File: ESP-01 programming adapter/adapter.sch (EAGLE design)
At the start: 7 parts

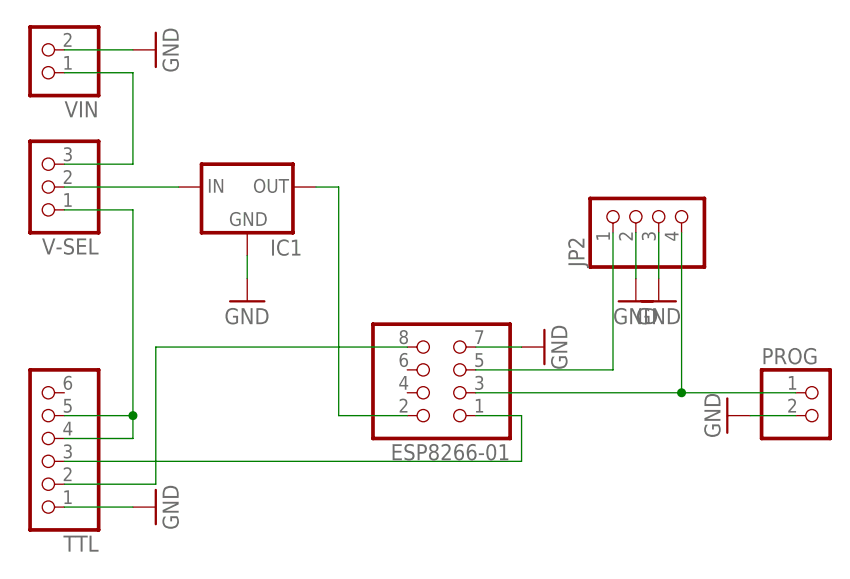
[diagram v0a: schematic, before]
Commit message: CH_PD
Added resistor and jumper to the CH_PD pin, allowing for either
connecting it to VCC for constant on, or to connect it to GPIO00 for
controlling it by code.
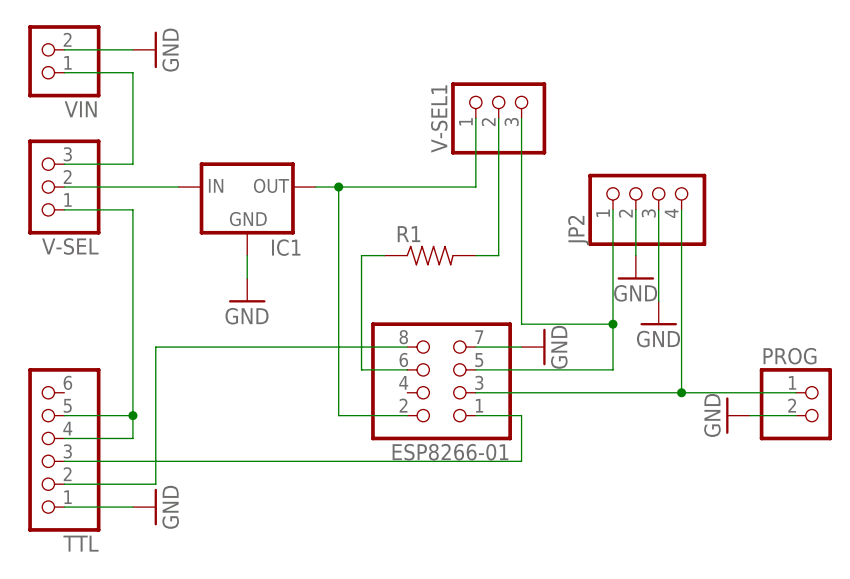
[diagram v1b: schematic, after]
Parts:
- added R1: (no value), SparkFun-Resistors:RESISTORAXIAL-0.3
- added V-SEL1: (no value), pinhead:PINHD-1X3
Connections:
- new net N$10: R1.2, V-SEL1.2
- new net N$8: ESP8266-01.6, R1.1
- net N$1: now also V-SEL1.1
- net N$9: now also V-SEL1.3
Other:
- moved on the sheet: JP2
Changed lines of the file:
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@@
 <part name="GND6" library="supply1" deviceset="GND" device=""/>
 <part name="GND7" library="supply1" deviceset="GND" device=""/>
+<part name="R1" library="SparkFun-Resistors" deviceset="RESISTOR" device="AXIAL-0.3"/>
+<part name="V-SEL1" library="pinhead" deviceset="PINHD-1X3" device=""/>
 </parts>
 <sheets>
@@
 <instance part="VIN" gate="G$1" x="2.54" y="53.34" rot="R180"/>
 <instance part="GND5" gate="1" x="15.24" y="53.34" rot="R90"/>
-<instance part="JP2" gate="A" x="71.12" y="35.56" rot="R90"/>
-<instance part="GND6" gate="1" x="68.58" y="25.4"/>
-<instance part="GND7" gate="1" x="71.12" y="25.4"/>
+<instance part="JP2" gate="A" x="71.12" y="38.1" rot="R90"/>
+<instance part="GND6" gate="1" x="68.58" y="27.94"/>
+<instance part="GND7" gate="1" x="71.12" y="22.86"/>
+<instance part="R1" gate="G$1" x="45.72" y="30.48"/>
+<instance part="V-SEL1" gate="A" x="53.34" y="48.26" rot="R90"/>
 </instances>
 <busses>
@@
 <pinref part="GND6" gate="1" pin="GND"/>
 <pinref part="JP2" gate="A" pin="2"/>
-<wire x1="68.58" y1="27.94" x2="68.58" y2="33.02" width="0.1524" layer="91"/>
+<wire x1="68.58" y1="30.48" x2="68.58" y2="35.56" width="0.1524" layer="91"/>
 </segment>
 <segment>
 <pinref part="GND7" gate="1" pin="GND"/>
 <pinref part="JP2" gate="A" pin="3"/>
-<wire x1="71.12" y1="27.94" x2="71.12" y2="33.02" width="0.1524" layer="91"/>
+<wire x1="71.12" y1="25.4" x2="71.12" y2="35.56" width="0.1524" layer="91"/>
 </segment>
 </net>
@@
 <pinref part="JP2" gate="A" pin="4"/>
 <wire x1="73.66" y1="15.24" x2="50.8" y2="15.24" width="0.1524" layer="91"/>
-<wire x1="73.66" y1="33.02" x2="73.66" y2="15.24" width="0.1524" layer="91"/>
+<wire x1="73.66" y1="35.56" x2="73.66" y2="15.24" width="0.1524" layer="91"/>
 <junction x="73.66" y="15.24"/>
 </segment>
@@
 <pinref part="IC1" gate="G$1" pin="OUT"/>
 <wire x1="35.56" y1="38.1" x2="33.02" y2="38.1" width="0.1524" layer="91"/>
+<wire x1="35.56" y1="38.1" x2="50.8" y2="38.1" width="0.1524" layer="91"/>
+<pinref part="V-SEL1" gate="A" pin="1"/>
+<wire x1="50.8" y1="38.1" x2="50.8" y2="45.72" width="0.1524" layer="91"/>
+<junction x="35.56" y="38.1"/>
 </segment>
 </net>
@@
 <pinref part="JP2" gate="A" pin="1"/>
 <wire x1="50.8" y1="17.78" x2="66.04" y2="17.78" width="0.1524" layer="91"/>
-<wire x1="66.04" y1="17.78" x2="66.04" y2="33.02" width="0.1524" layer="91"/>
+<wire x1="66.04" y1="17.78" x2="66.04" y2="22.86" width="0.1524" layer="91"/>
+<pinref part="V-SEL1" gate="A" pin="3"/>
+<wire x1="66.04" y1="22.86" x2="66.04" y2="35.56" width="0.1524" layer="91"/>
+<wire x1="66.04" y1="22.86" x2="55.88" y2="22.86" width="0.1524" layer="91"/>
+<wire x1="55.88" y1="22.86" x2="55.88" y2="45.72" width="0.1524" layer="91"/>
+<junction x="66.04" y="22.86"/>
 </segment>
 </net>
+<net name="N$8" class="0">
+<segment>
+<pinref part="ESP8266-01" gate="A" pin="6"/>
+<wire x1="43.18" y1="17.78" x2="38.1" y2="17.78" width="0.1524" layer="91"/>
+<wire x1="38.1" y1="17.78" x2="38.1" y2="30.48" width="0.1524" layer="91"/>
+<pinref part="R1" gate="G$1" pin="1"/>
+<wire x1="38.1" y1="30.48" x2="40.64" y2="30.48" width="0.1524" layer="91"/>
+</segment>
+</net>
+<net name="N$10" class="0">
+<segment>
+<pinref part="V-SEL1" gate="A" pin="2"/>
+<wire x1="53.34" y1="45.72" x2="53.34" y2="30.48" width="0.1524" layer="91"/>
+<pinref part="R1" gate="G$1" pin="2"/>
+<wire x1="53.34" y1="30.48" x2="50.8" y2="30.48" width="0.1524" layer="91"/>
+</segment>
+</net>

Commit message: Voltage regulator pin out
Changed pin out on the voltage regulator to fit TI LM1117 TO-220 package

http://www.ti.com/lit/ds/symlink/lm1117-n.pdf
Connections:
- removed net N$6: IC1.IN, V-SEL.2
- new net N$11: IC1.OUT, V-SEL.2
- net GND: now also IC1.IN; no longer IC1.GND
- net N$1: now also IC1.GND; no longer IC1.OUT
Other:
- moved on the sheet: IC1
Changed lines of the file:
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@@
 <part name="ESP8266-01" library="pinhead" deviceset="PINHD-2X4" device=""/>
 <part name="IC1" library="SparkFun-PowerIC" deviceset="V_REG_78XX" device="SIDE"/>
-<part name="GND1" library="supply1" deviceset="GND" device=""/>
 <part name="GND2" library="supply1" deviceset="GND" device=""/>
 <part name="GND3" library="supply1" deviceset="GND" device=""/>
@@
 <part name="R1" library="SparkFun-Resistors" deviceset="RESISTOR" device="AXIAL-0.3"/>
 <part name="V-SEL1" library="pinhead" deviceset="PINHD-1X3" device=""/>
+<part name="GND8" library="supply1" deviceset="GND" device=""/>
 </parts>
 <sheets>
@@
 <instance part="TTL" gate="A" x="2.54" y="10.16" rot="R180"/>
 <instance part="ESP8266-01" gate="A" x="48.26" y="17.78" rot="R180"/>
-<instance part="IC1" gate="G$1" x="25.4" y="38.1"/>
-<instance part="GND1" gate="1" x="25.4" y="25.4"/>
+<instance part="IC1" gate="G$1" x="25.4" y="40.64"/>
 <instance part="GND2" gate="1" x="15.24" y="2.54" rot="R90"/>
 <instance part="GND3" gate="1" x="58.42" y="20.32" rot="R90"/>
@@
 <instance part="R1" gate="G$1" x="45.72" y="30.48"/>
 <instance part="V-SEL1" gate="A" x="53.34" y="48.26" rot="R90"/>
+<instance part="GND8" gate="1" x="17.78" y="30.48"/>
 </instances>
 <busses>
@@
 <nets>
 <net name="GND" class="0">
-<segment>
-<pinref part="GND1" gate="1" pin="GND"/>
-<pinref part="IC1" gate="G$1" pin="GND"/>
-<wire x1="25.4" y1="27.94" x2="25.4" y2="30.48" width="0.1524" layer="91"/>
-</segment>
 <segment>
 <pinref part="TTL" gate="A" pin="1"/>
@@
 <pinref part="JP2" gate="A" pin="3"/>
 <wire x1="71.12" y1="25.4" x2="71.12" y2="35.56" width="0.1524" layer="91"/>
+</segment>
+<segment>
+<pinref part="GND8" gate="1" pin="GND"/>
+<wire x1="17.78" y1="33.02" x2="17.78" y2="40.64" width="0.1524" layer="91"/>
+<pinref part="IC1" gate="G$1" pin="IN"/>
 </segment>
 </net>
@@
 <pinref part="ESP8266-01" gate="A" pin="2"/>
 <wire x1="43.18" y1="12.7" x2="35.56" y2="12.7" width="0.1524" layer="91"/>
-<wire x1="35.56" y1="12.7" x2="35.56" y2="38.1" width="0.1524" layer="91"/>
-<pinref part="IC1" gate="G$1" pin="OUT"/>
-<wire x1="35.56" y1="38.1" x2="33.02" y2="38.1" width="0.1524" layer="91"/>
+<wire x1="35.56" y1="12.7" x2="35.56" y2="27.94" width="0.1524" layer="91"/>
+<wire x1="35.56" y1="27.94" x2="35.56" y2="38.1" width="0.1524" layer="91"/>
 <wire x1="35.56" y1="38.1" x2="50.8" y2="38.1" width="0.1524" layer="91"/>
 <pinref part="V-SEL1" gate="A" pin="1"/>
 <wire x1="50.8" y1="38.1" x2="50.8" y2="45.72" width="0.1524" layer="91"/>
-<junction x="35.56" y="38.1"/>
+<pinref part="IC1" gate="G$1" pin="GND"/>
+<wire x1="25.4" y1="33.02" x2="25.4" y2="27.94" width="0.1524" layer="91"/>
+<wire x1="25.4" y1="27.94" x2="35.56" y2="27.94" width="0.1524" layer="91"/>
+<junction x="35.56" y="27.94"/>
 </segment>
 </net>
@@
 <wire x1="12.7" y1="10.16" x2="12.7" y2="12.7" width="0.1524" layer="91"/>
 <junction x="12.7" y="12.7"/>
-</segment>
-</net>
-<net name="N$6" class="0">
-<segment>
-<pinref part="V-SEL" gate="A" pin="2"/>
-<wire x1="5.08" y1="38.1" x2="17.78" y2="38.1" width="0.1524" layer="91"/>
-<pinref part="IC1" gate="G$1" pin="IN"/>
 </segment>
 </net>
@@
 </segment>
 </net>
+<net name="N$11" class="0">
+<segment>
+<pinref part="V-SEL" gate="A" pin="2"/>
+<wire x1="5.08" y1="38.1" x2="15.24" y2="38.1" width="0.1524" layer="91"/>
+<wire x1="15.24" y1="38.1" x2="15.24" y2="45.72" width="0.1524" layer="91"/>
+<pinref part="IC1" gate="G$1" pin="OUT"/>
+<wire x1="15.24" y1="45.72" x2="33.02" y2="45.72" width="0.1524" layer="91"/>
+<wire x1="33.02" y1="45.72" x2="33.02" y2="40.64" width="0.1524" layer="91"/>
+</segment>
+</net>

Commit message: CH_PD
Pin connected to GPIO00 instead of 02, so GPIO02 is free to do external
triggers.
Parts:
- renumbered V-SEL1 to WIFI-SEL
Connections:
- removed net N$4: ESP8266-01.3, JP2.4, PROG.1
- new net N$6: ESP8266-01.3, JP2.4, PROG.1, WIFI-SEL.3
- net N$9: no longer WIFI-SEL.3
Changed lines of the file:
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@@
 <part name="GND7" library="supply1" deviceset="GND" device=""/>
 <part name="R1" library="SparkFun-Resistors" deviceset="RESISTOR" device="AXIAL-0.3"/>
-<part name="V-SEL1" library="pinhead" deviceset="PINHD-1X3" device=""/>
+<part name="WIFI-SEL" library="pinhead" deviceset="PINHD-1X3" device=""/>
 <part name="GND8" library="supply1" deviceset="GND" device=""/>
 </parts>
@@
 <instance part="GND7" gate="1" x="71.12" y="22.86"/>
 <instance part="R1" gate="G$1" x="45.72" y="30.48"/>
-<instance part="V-SEL1" gate="A" x="53.34" y="48.26" rot="R90"/>
+<instance part="WIFI-SEL" gate="A" x="53.34" y="48.26" rot="R90"/>
 <instance part="GND8" gate="1" x="17.78" y="30.48"/>
 </instances>
@@
 </segment>
 </net>
-<net name="N$4" class="0">
-<segment>
-<pinref part="ESP8266-01" gate="A" pin="3"/>
-<pinref part="PROG" gate="G$1" pin="1"/>
-<wire x1="86.36" y1="15.24" x2="73.66" y2="15.24" width="0.1524" layer="91"/>
-<pinref part="JP2" gate="A" pin="4"/>
-<wire x1="73.66" y1="15.24" x2="50.8" y2="15.24" width="0.1524" layer="91"/>
-<wire x1="73.66" y1="35.56" x2="73.66" y2="15.24" width="0.1524" layer="91"/>
-<junction x="73.66" y="15.24"/>
-</segment>
-</net>
 <net name="N$1" class="0">
 <segment>
@@
 <wire x1="35.56" y1="27.94" x2="35.56" y2="38.1" width="0.1524" layer="91"/>
 <wire x1="35.56" y1="38.1" x2="50.8" y2="38.1" width="0.1524" layer="91"/>
-<pinref part="V-SEL1" gate="A" pin="1"/>
+<pinref part="WIFI-SEL" gate="A" pin="1"/>
 <wire x1="50.8" y1="38.1" x2="50.8" y2="45.72" width="0.1524" layer="91"/>
 <pinref part="IC1" gate="G$1" pin="GND"/>
@@
 <pinref part="JP2" gate="A" pin="1"/>
 <wire x1="50.8" y1="17.78" x2="66.04" y2="17.78" width="0.1524" layer="91"/>
-<wire x1="66.04" y1="17.78" x2="66.04" y2="22.86" width="0.1524" layer="91"/>
-<pinref part="V-SEL1" gate="A" pin="3"/>
-<wire x1="66.04" y1="22.86" x2="66.04" y2="35.56" width="0.1524" layer="91"/>
-<wire x1="66.04" y1="22.86" x2="55.88" y2="22.86" width="0.1524" layer="91"/>
-<wire x1="55.88" y1="22.86" x2="55.88" y2="45.72" width="0.1524" layer="91"/>
-<junction x="66.04" y="22.86"/>
+<wire x1="66.04" y1="17.78" x2="66.04" y2="35.56" width="0.1524" layer="91"/>
 </segment>
 </net>
@@
 <net name="N$10" class="0">
 <segment>
-<pinref part="V-SEL1" gate="A" pin="2"/>
+<pinref part="WIFI-SEL" gate="A" pin="2"/>
 <wire x1="53.34" y1="45.72" x2="53.34" y2="30.48" width="0.1524" layer="91"/>
 <pinref part="R1" gate="G$1" pin="2"/>
@@
 </segment>
 </net>
+<net name="N$6" class="0">
+<segment>
+<pinref part="WIFI-SEL" gate="A" pin="3"/>
+<wire x1="55.88" y1="27.94" x2="55.88" y2="45.72" width="0.1524" layer="91"/>
+<wire x1="55.88" y1="27.94" x2="63.5" y2="27.94" width="0.1524" layer="91"/>
+<pinref part="ESP8266-01" gate="A" pin="3"/>
+<pinref part="PROG" gate="G$1" pin="1"/>
+<wire x1="86.36" y1="15.24" x2="73.66" y2="15.24" width="0.1524" layer="91"/>
+<pinref part="JP2" gate="A" pin="4"/>
+<wire x1="73.66" y1="15.24" x2="63.5" y2="15.24" width="0.1524" layer="91"/>
+<wire x1="63.5" y1="15.24" x2="50.8" y2="15.24" width="0.1524" layer="91"/>
+<wire x1="73.66" y1="35.56" x2="73.66" y2="15.24" width="0.1524" layer="91"/>
+<junction x="73.66" y="15.24"/>
+<wire x1="63.5" y1="27.94" x2="63.5" y2="15.24" width="0.1524" layer="91"/>
+<junction x="63.5" y="15.24"/>
+</segment>
+</net>
